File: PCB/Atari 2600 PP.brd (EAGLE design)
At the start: 58.5 x 61 mm, 16 parts, among them U1A SN74AHCT125N, U2A SN74AHCT125N, U3A SN74AHCT125N

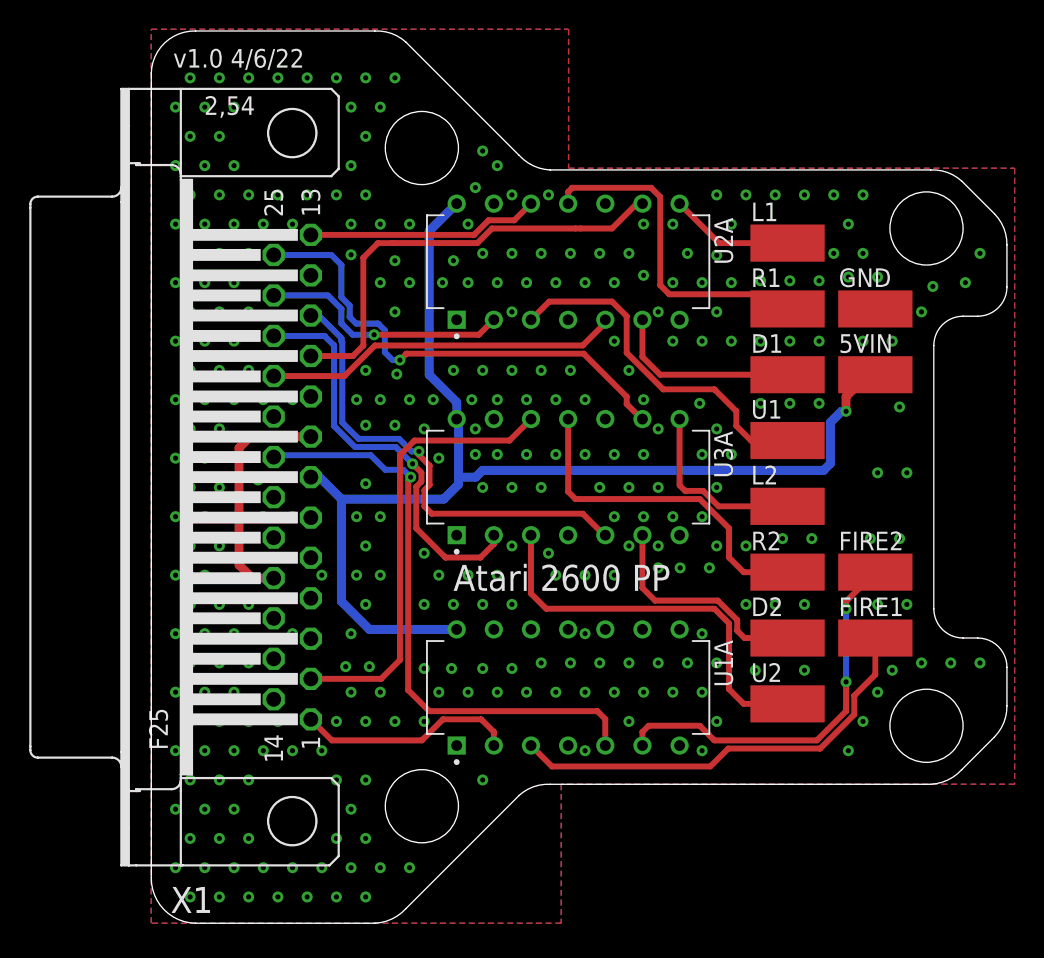
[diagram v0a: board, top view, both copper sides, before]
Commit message: Added exposed GND plane at DB25 anchors
All PCBs have been update to have exposed GND plane pads for the DB25 anchor points.

This resolves Issue 54
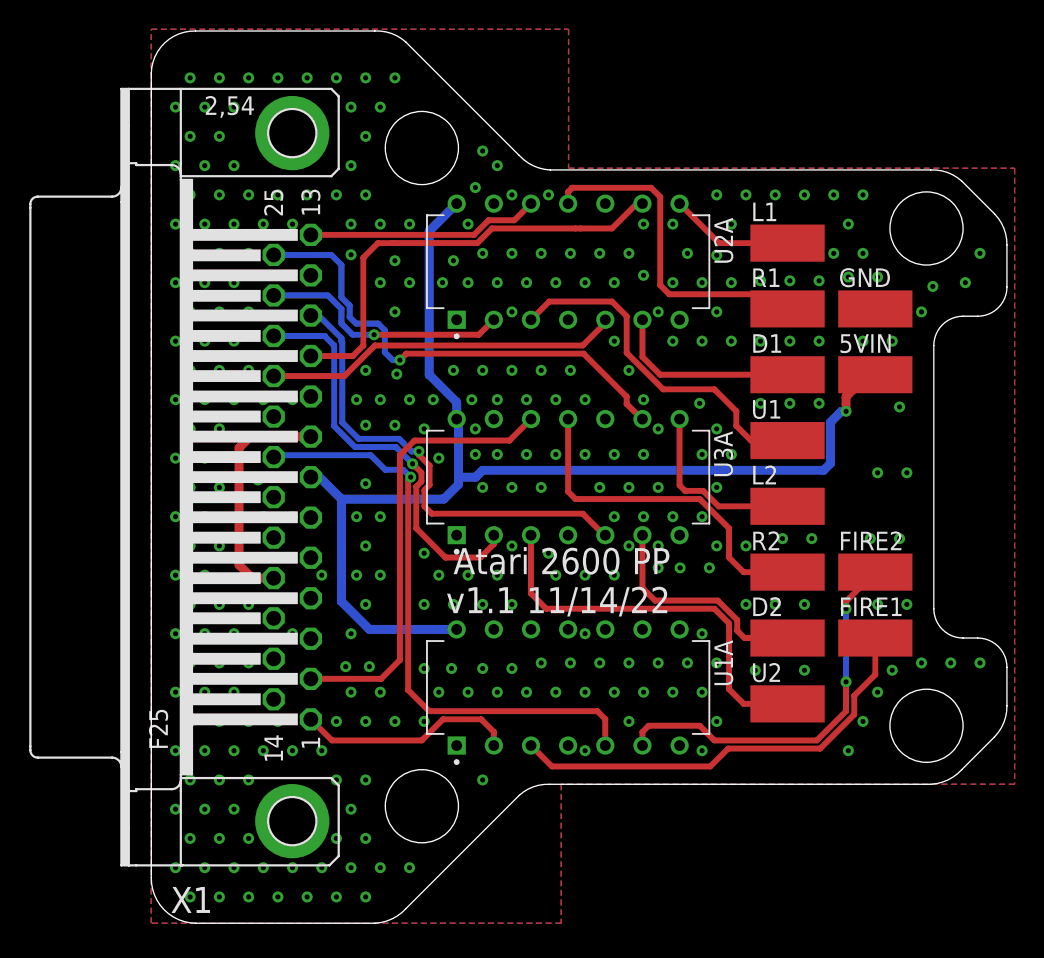
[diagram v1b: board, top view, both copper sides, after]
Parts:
- X1: device SparkFun-Retired:F25H -> SparkFun-Retired:F25HP
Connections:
- net GND: now also X1.GND1, X1.GND2
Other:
- board text added: "Atari 2600 PP v1.1 11/14/22"
- board text removed: "Atari 2600 PP"
- board text removed: "v1.0 4/6/22"

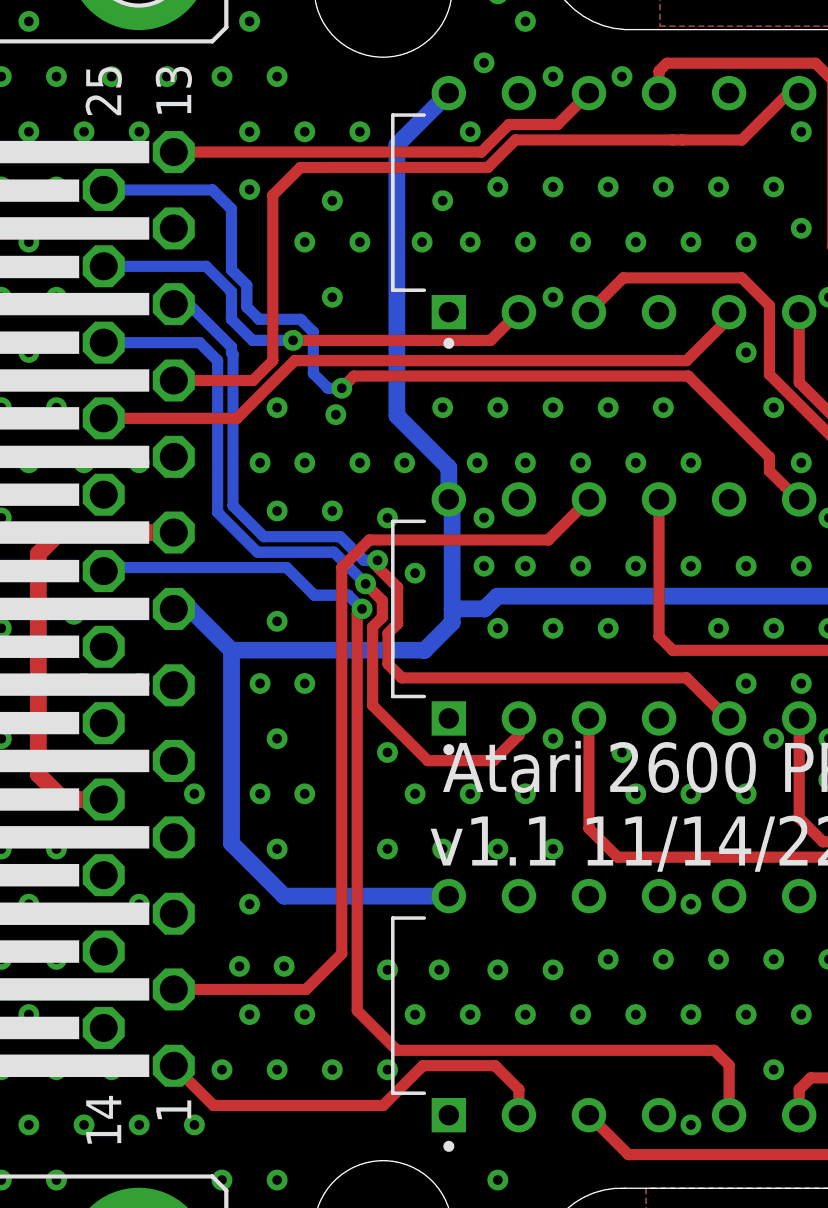
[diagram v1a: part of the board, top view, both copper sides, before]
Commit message: Silkscreen Update, Library Add, Datasheet Add
Updated the silkscreen on all PCBs that used the SN74 components as there was not orientation marker on the silkscreen.

Added Modified SN74 libraries and VB Cable Pinout image
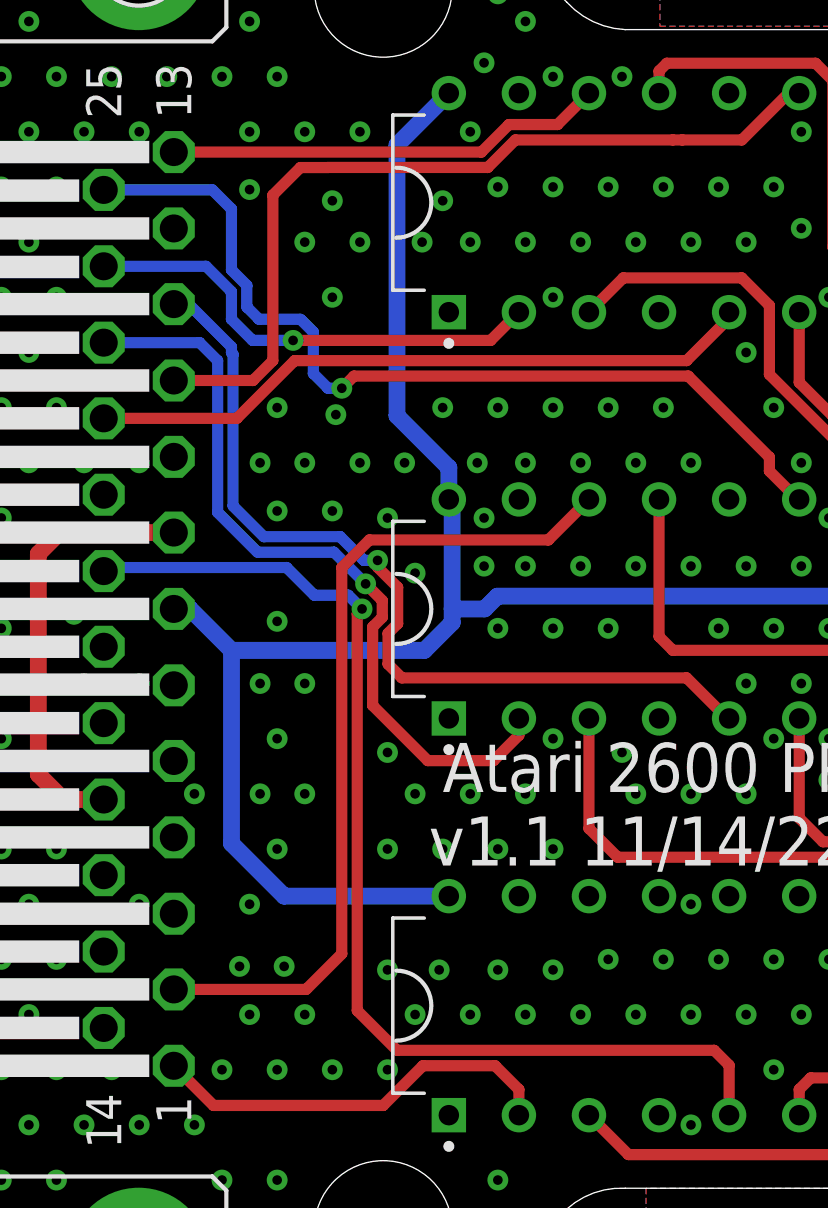
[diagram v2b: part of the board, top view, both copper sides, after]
